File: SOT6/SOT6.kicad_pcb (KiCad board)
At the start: 2 copper layers, 11.4 x 8.9 mm, 5 parts, among them J1 Conn_01x03, J2 Conn_01x03

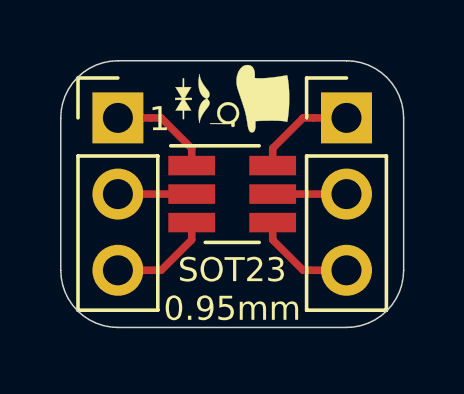
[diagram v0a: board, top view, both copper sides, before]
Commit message: Silkscreens and sizes updated
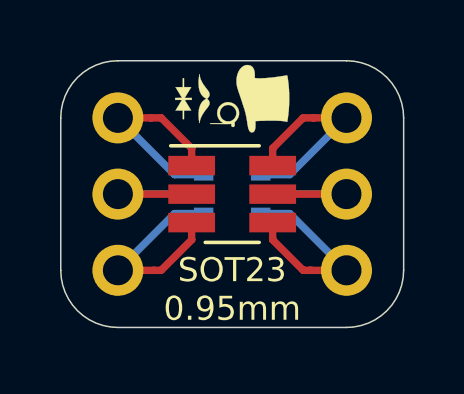
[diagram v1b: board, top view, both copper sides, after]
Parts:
- removed the G*** at (158.8, 96.5)
- added G***: LOGO, logo:logo38x53, B.Cu at (158.8, 93.3)
- added J4: Conn_02x03_Counter_Clockwise, Package_TO_SOT_SMD:SOT-363_SC-70-6, B.Cu at (158.8, 96.5)
- renumbered SOT23 to J3
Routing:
- net Net-(J2-Pad3): track 3.46 -> 7.10 mm
- net Net-(J2-Pad1): track 3.46 -> 7.10 mm
- net Net-(J1-Pad3): track 3.46 -> 7.10 mm
- net Net-(J1-Pad1): track 3.46 -> 7.10 mm
- net Net-(J2-Pad2): track 2.46 -> 5.32 mm
- net Net-(J1-Pad2): track 2.46 -> 5.32 mm
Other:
- board text added: "SC-70 0.65mm"
- board text removed: "1"

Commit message: Dimensions Added And TQFP64 Added
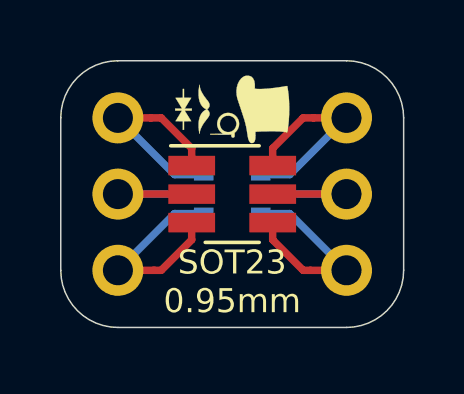
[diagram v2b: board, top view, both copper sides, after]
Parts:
- moved G*** 0.38 mm to (158.8, 93.7)
- moved G*** 0.36 mm to (158.8, 93.7)
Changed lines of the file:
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@@
   (general
     (thickness 1.6)
-    (drawings 12)
+    (drawings 14)
     (tracks 28)
     (zones 0)
@@
     (34 B.Paste user hide)
     (35 F.Paste user hide)
-    (36 B.SilkS user)
+    (36 B.SilkS user hide)
     (37 F.SilkS user)
     (38 B.Mask user hide)
@@
   )
   (module logo:logo38x53 (layer B.Cu)
-    (at 158.75 93.345 90)
+    (at 158.7754 93.726 90)
     (fp_text reference G*** (at 0 0 270) (layer B.SilkS) hide
       (effects (font (size 1.524 1.524) (thickness 0.3)) (justify mirror))
@@
   )
   (module logo:logo38x53 (layer F.Cu)
-    (at 158.75 93.345 270)
+    (at 158.75 93.7006 270)
     (fp_text reference G*** (at 0 0 90) (layer F.SilkS) hide
       (effects (font (size 1.524 1.524) (thickness 0.3)))
@@
     )
   )
+  (dimension 5.08 (width 0.15) (layer Dwgs.User)
+    (gr_text "5.080 mm" (at 168.305 96.52 270) (layer Dwgs.User)
+      (effects (font (size 1 1) (thickness 0.15)) hide)
+    )
+    (feature1 (pts (xy 162.56 99.06) (xy 167.591421 99.06)))
+    (feature2 (pts (xy 162.56 93.98) (xy 167.591421 93.98)))
+    (crossbar (pts (xy 167.005 93.98) (xy 167.005 99.06)))
+    (arrow1a (pts (xy 167.005 99.06) (xy 166.418579 97.933496)))
+    (arrow1b (pts (xy 167.005 99.06) (xy 167.591421 97.933496)))
+    (arrow2a (pts (xy 167.005 93.98) (xy 166.418579 95.106504)))
+    (arrow2b (pts (xy 167.005 93.98) (xy 167.591421 95.106504)))
+  )
+  (dimension 7.62 (width 0.15) (layer Dwgs.User)
+    (gr_text "7.620 mm" (at 158.75 88.743) (layer Dwgs.User)
+      (effects (font (size 1 1) (thickness 0.15)) hide)
+    )
+    (feature1 (pts (xy 162.56 93.98) (xy 162.56 89.456579)))
+    (feature2 (pts (xy 154.94 93.98) (xy 154.94 89.456579)))
+    (crossbar (pts (xy 154.94 90.043) (xy 162.56 90.043)))
+    (arrow1a (pts (xy 162.56 90.043) (xy 161.433496 90.629421)))
+    (arrow1b (pts (xy 162.56 90.043) (xy 161.433496 89.456579)))
+    (arrow2a (pts (xy 154.94 90.043) (xy 156.066504 90.629421)))
+    (arrow2b (pts (xy 154.94 90.043) (xy 156.066504 89.456579)))
+  )
   (dimension 8.89 (width 0.15) (layer Dwgs.User)
-    (gr_text "8.890 mm" (at 170.591 96.52 270) (layer Dwgs.User)
-      (effects (font (size 1 1) (thickness 0.15)))
-    )
-    (feature1 (pts (xy 164.465 100.965) (xy 169.877421 100.965)))
-    (feature2 (pts (xy 164.465 92.075) (xy 169.877421 92.075)))
-    (crossbar (pts (xy 169.291 92.075) (xy 169.291 100.965)))
-    (arrow1a (pts (xy 169.291 100.965) (xy 168.704579 99.838496)))
-    (arrow1b (pts (xy 169.291 100.965) (xy 169.877421 99.838496)))
-    (arrow2a (pts (xy 169.291 92.075) (xy 168.704579 93.201504)))
-    (arrow2b (pts (xy 169.291 92.075) (xy 169.877421 93.201504)))
+    (gr_text "8.890 mm" (at 171.353 96.52 270) (layer Dwgs.User)
+      (effects (font (size 1 1) (thickness 0.15)) hide)
+    )
+    (feature1 (pts (xy 162.56 100.965) (xy 170.639421 100.965)))
+    (feature2 (pts (xy 162.56 92.075) (xy 170.639421 92.075)))
+    (crossbar (pts (xy 170.053 92.075) (xy 170.053 100.965)))
+    (arrow1a (pts (xy 170.053 100.965) (xy 169.466579 99.838496)))
+    (arrow1b (pts (xy 170.053 100.965) (xy 170.639421 99.838496)))
+    (arrow2a (pts (xy 170.053 92.075) (xy 169.466579 93.201504)))
+    (arrow2b (pts (xy 170.053 92.075) (xy 170.639421 93.201504)))
   )
   (dimension 11.43 (width 0.15) (layer Dwgs.User)
-    (gr_text "11.430 mm" (at 158.75 86.711) (layer Dwgs.User)
-      (effects (font (size 1 1) (thickness 0.15)))
-    )
-    (feature1 (pts (xy 164.465 92.075) (xy 164.465 87.424579)))
-    (feature2 (pts (xy 153.035 92.075) (xy 153.035 87.424579)))
-    (crossbar (pts (xy 153.035 88.011) (xy 164.465 88.011)))
-    (arrow1a (pts (xy 164.465 88.011) (xy 163.338496 88.597421)))
-    (arrow1b (pts (xy 164.465 88.011) (xy 163.338496 87.424579)))
-    (arrow2a (pts (xy 153.035 88.011) (xy 154.161504 88.597421)))
-    (arrow2b (pts (xy 153.035 88.011) (xy 154.161504 87.424579)))
-  )
-  (gr_text "SC-70\n0.65mm" (at 158.75 99.695) (layer B.SilkS)
+    (gr_text "11.430 mm" (at 158.75 86.203) (layer Dwgs.User)
+      (effects (font (size 1 1) (thickness 0.15)) hide)
+    )
+    (feature1 (pts (xy 164.465 93.98) (xy 164.465 86.916579)))
+    (feature2 (pts (xy 153.035 93.98) (xy 153.035 86.916579)))
+    (crossbar (pts (xy 153.035 87.503) (xy 164.465 87.503)))
+    (arrow1a (pts (xy 164.465 87.503) (xy 163.338496 88.089421)))
+    (arrow1b (pts (xy 164.465 87.503) (xy 163.338496 86.916579)))
+    (arrow2a (pts (xy 153.035 87.503) (xy 154.161504 88.089421)))
+    (arrow2b (pts (xy 153.035 87.503) (xy 154.161504 86.916579)))
+  )
+  (gr_text "SC-70\n0.65mm" (at 158.7246 99.441) (layer B.SilkS)
     (effects (font (size 0.8 0.8) (thickness 0.15)) (justify mirror))
   )
-  (gr_text "SOT23\n0.95mm" (at 158.75 99.695) (layer F.SilkS)
+  (gr_text "SOT23\n0.95mm" (at 158.75 99.441) (layer F.SilkS)
     (effects (font (size 0.8 0.8) (thickness 0.15)))
   )

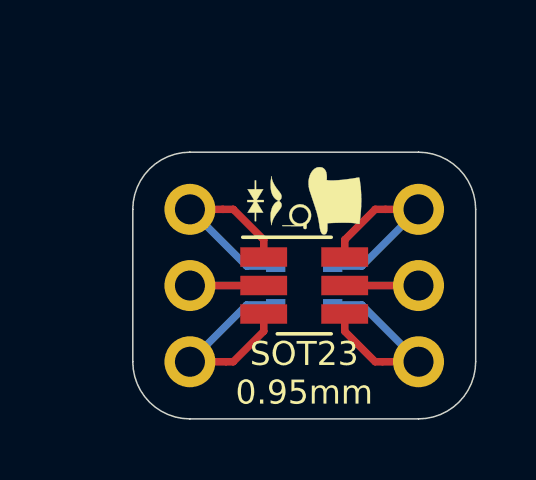
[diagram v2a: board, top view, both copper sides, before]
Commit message: Numbering Orientation Edited
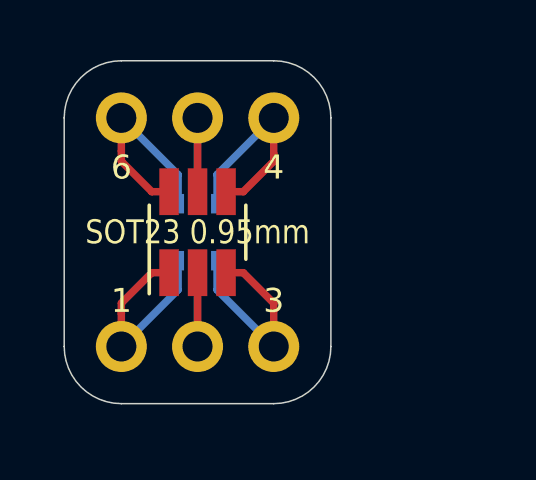
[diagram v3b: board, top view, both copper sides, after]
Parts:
- removed the G*** at (158.8, 93.7)
- moved J1 10.4 mm to (152.7, 90.9), turned to 90 degrees
- moved G*** 6.45 mm to (152.4, 94.7), turned to 180 degrees
- moved J2 5.11 mm to (152.7, 98.6), turned to 90 degrees
- moved J3 3.98 mm to (155.2, 94.7), turned to 90 degrees
- moved J4 3.98 mm to (155.2, 94.7), turned to 270 degrees
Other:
- board size 11.4 x 8.9 mm -> 8.9 x 11.4 mm
- board text added: "1"
- board text added: "3"
- board text added: "4"
- board text added: "6"

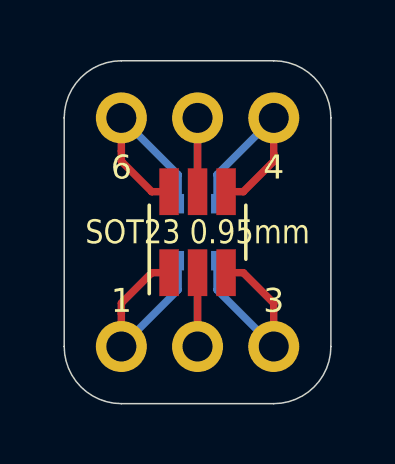
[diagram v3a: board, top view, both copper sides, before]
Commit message: Silkscreen Edits
Dimensions moved to Drawings Layer
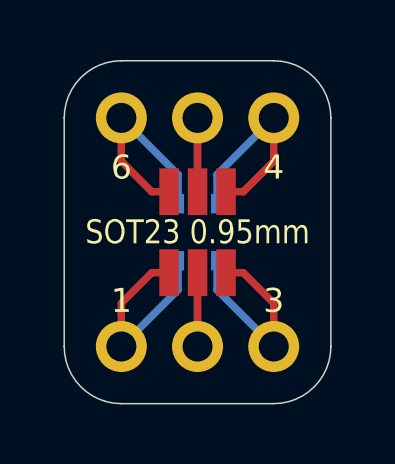
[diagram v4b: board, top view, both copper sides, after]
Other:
- rule pad_to_mask_clearance: 0.051 -> 0
- rule solder_mask_min_width: 0.25 -> 0.1
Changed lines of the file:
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@@
   (page A4)
   (layers
-    (0 F.Cu signal hide)
+    (0 F.Cu signal)
     (31 B.Cu signal)
     (32 B.Adhes user)
@@
     (pad_size 1.7 1.7)
     (pad_drill 1)
-    (pad_to_mask_clearance 0.051)
-    (solder_mask_min_width 0.25)
+    (pad_to_mask_clearance 0)
+    (solder_mask_min_width 0.1)
     (aux_axis_origin 0 0)
     (visible_elements 7FFFFFFF)
@@
       (usegerberadvancedattributes false)
       (creategerberjobfile false)
-      (excludeedgelayer false)
+      (excludeedgelayer true)
       (linewidth 0.100000)
       (plotframeref false)
       (viasonmask false)
       (mode 1)
-      (useauxorigin false)
+      (useauxorigin true)
       (hpglpennumber 1)
       (hpglpenspeed 20)
@@
       (drillshape 0)
       (scaleselection 1)
-      (outputdirectory "../../Gerbers/SOT23/"))
+      (outputdirectory "C:/Users/elisha3/Desktop/GitHub/Gerbers/SOT6/"))
   )
   (net 0 "")
@@
     (add_net "Net-(J2-Pad2)")
     (add_net "Net-(J2-Pad3)")
+  )
+  (module Package_TO_SOT_SMD:SOT-23-6_Handsoldering (layer F.Cu)
+    (at 155.194 94.742 90)
+    (descr "6-pin SOT-23 package, Handsoldering")
+    (tags "SOT-23-6 Handsoldering")
+    (attr smd)
+    (fp_text reference J3 (at 0 -2.9 90) (layer F.SilkS) hide
+      (effects (font (size 1 1) (thickness 0.15)))
+    )
+    (fp_text value Conn_02x03_Counter_Clockwise (at 0 2.9 90) (layer F.Fab)
+      (effects (font (size 1 1) (thickness 0.15)))
+    )
+    (fp_line (start 0.9 -1.55) (end 0.9 1.55) (layer F.Fab) (width 0.1))
+    (fp_line (start 0.9 1.55) (end -0.9 1.55) (layer F.Fab) (width 0.1))
+    (fp_line (start -0.9 -0.9) (end -0.9 1.55) (layer F.Fab) (width 0.1))
+    (fp_line (start 0.9 -1.55) (end -0.25 -1.55) (layer F.Fab) (width 0.1))
+    (fp_line (start -0.9 -0.9) (end -0.25 -1.55) (layer F.Fab) (width 0.1))
+    (fp_line (start -2.4 -1.8) (end 2.4 -1.8) (layer F.CrtYd) (width 0.05))
+    (fp_line (start 2.4 -1.8) (end 2.4 1.8) (layer F.CrtYd) (width 0.05))
+    (fp_line (start 2.4 1.8) (end -2.4 1.8) (layer F.CrtYd) (width 0.05))
+    (fp_line (start -2.4 1.8) (end -2.4 -1.8) (layer F.CrtYd) (width 0.05))
+    (fp_text user %R (at 0 0 180) (layer F.Fab)
+      (effects (font (size 0.5 0.5) (thickness 0.075)))
+    )
+    (pad 5 smd rect (at 1.35 0 90) (size 1.56 0.65) (layers F.Cu F.Paste F.Mask)
+      (net 2 "Net-(J1-Pad2)"))
+    (pad 6 smd rect (at 1.35 -0.95 90) (size 1.56 0.65) (layers F.Cu F.Paste F.Mask)
+      (net 3 "Net-(J1-Pad1)"))
+    (pad 4 smd rect (at 1.35 0.95 90) (size 1.56 0.65) (layers F.Cu F.Paste F.Mask)
+      (net 1 "Net-(J1-Pad3)"))
+    (pad 3 smd rect (at -1.35 0.95 90) (size 1.56 0.65) (layers F.Cu F.Paste F.Mask)
+      (net 4 "Net-(J2-Pad3)"))
+    (pad 2 smd rect (at -1.35 0 90) (size 1.56 0.65) (layers F.Cu F.Paste F.Mask)
+      (net 5 "Net-(J2-Pad2)"))
+    (pad 1 smd rect (at -1.35 -0.95 90) (size 1.56 0.65) (layers F.Cu F.Paste F.Mask)
+      (net 6 "Net-(J2-Pad1)"))
+    (model ${KISYS3DMOD}/Package_TO_SOT_SMD.3dshapes/SOT-23-6.wrl
+      (at (xyz 0 0 0))
+      (scale (xyz 1 1 1))
+      (rotate (xyz 0 0 0))
+    )
   )
   (module logo:logo38x53 (layer B.Cu)
@@
     )
   )
-  (module Package_TO_SOT_SMD:SOT-23-6_Handsoldering (layer F.Cu)
-    (at 155.194 94.742 90)
-    (descr "6-pin SOT-23 package, Handsoldering")
-    (tags "SOT-23-6 Handsoldering")
-    (attr smd)
-    (fp_text reference J3 (at 0 -2.9 90) (layer F.SilkS) hide
-      (effects (font (size 1 1) (thickness 0.15)))
-    )
-    (fp_text value Conn_02x03_Counter_Clockwise (at 0 2.9 90) (layer F.Fab)
-      (effects (font (size 1 1) (thickness 0.15)))
-    )
-    (fp_line (start 0.9 -1.55) (end 0.9 1.55) (layer F.Fab) (width 0.1))
-    (fp_line (start 0.9 1.55) (end -0.9 1.55) (layer F.Fab) (width 0.1))
-    (fp_line (start -0.9 -0.9) (end -0.9 1.55) (layer F.Fab) (width 0.1))
-    (fp_line (start 0.9 -1.55) (end -0.25 -1.55) (layer F.Fab) (width 0.1))
-    (fp_line (start -0.9 -0.9) (end -0.25 -1.55) (layer F.Fab) (width 0.1))
-    (fp_line (start -2.4 -1.8) (end 2.4 -1.8) (layer F.CrtYd) (width 0.05))
-    (fp_line (start 2.4 -1.8) (end 2.4 1.8) (layer F.CrtYd) (width 0.05))
-    (fp_line (start 2.4 1.8) (end -2.4 1.8) (layer F.CrtYd) (width 0.05))
-    (fp_line (start -2.4 1.8) (end -2.4 -1.8) (layer F.CrtYd) (width 0.05))
-    (fp_line (start 0.9 -1.61) (end -2.05 -1.61) (layer F.SilkS) (width 0.12))
-    (fp_line (start -0.9 1.61) (end 0.9 1.61) (layer F.SilkS) (width 0.12))
-    (fp_text user %R (at 0 0) (layer F.Fab)
-      (effects (font (size 0.5 0.5) (thickness 0.075)))
-    )
-    (pad 5 smd rect (at 1.35 0 90) (size 1.56 0.65) (layers F.Cu F.Paste F.Mask)
-      (net 2 "Net-(J1-Pad2)"))
-    (pad 6 smd rect (at 1.35 -0.95 90) (size 1.56 0.65) (layers F.Cu F.Paste F.Mask)
-      (net 3 "Net-(J1-Pad1)"))
-    (pad 4 smd rect (at 1.35 0.95 90) (size 1.56 0.65) (layers F.Cu F.Paste F.Mask)
-      (net 1 "Net-(J1-Pad3)"))
-    (pad 3 smd rect (at -1.35 0.95 90) (size 1.56 0.65) (layers F.Cu F.Paste F.Mask)
-      (net 4 "Net-(J2-Pad3)"))
-    (pad 2 smd rect (at -1.35 0 90) (size 1.56 0.65) (layers F.Cu F.Paste F.Mask)
-      (net 5 "Net-(J2-Pad2)"))
-    (pad 1 smd rect (at -1.35 -0.95 90) (size 1.56 0.65) (layers F.Cu F.Paste F.Mask)
-      (net 6 "Net-(J2-Pad1)"))
-    (model ${KISYS3DMOD}/Package_TO_SOT_SMD.3dshapes/SOT-23-6.wrl
-      (at (xyz 0 0 0))
-      (scale (xyz 1 1 1))
-      (rotate (xyz 0 0 0))
-    )
-  )
   (gr_text 6 (at 152.654 92.583) (layer F.SilkS)
     (effects (font (size 0.8 0.8) (thickness 0.13)))
@@
     (effects (font (size 0.8 0.8) (thickness 0.13)))
   )
-  (dimension 5.08 (width 0.15) (layer F.SilkS)
-    (gr_text "5.080 mm" (at 155.194 85.187) (layer F.SilkS)
+  (dimension 5.08 (width 0.15) (layer Dwgs.User)
+    (gr_text "5.080 mm" (at 155.194 85.187) (layer Dwgs.User)
       (effects (font (size 1 1) (thickness 0.15)) hide)
     )
@@
     (arrow2b (pts (xy 152.654 86.487) (xy 153.780504 85.900579)))
   )
-  (dimension 7.62 (width 0.15) (layer F.SilkS)
-    (gr_text "7.620 mm" (at 147.417 94.742 90) (layer F.SilkS)
+  (dimension 7.62 (width 0.15) (layer Dwgs.User)
+    (gr_text "7.620 mm" (at 147.417 94.742 90) (layer Dwgs.User)
       (effects (font (size 1 1) (thickness 0.15)) hide)
     )
@@
     (arrow2b (pts (xy 148.717 98.552) (xy 148.130579 97.425496)))
   )
-  (dimension 8.89 (width 0.15) (layer F.SilkS)
-    (gr_text "8.890 mm" (at 155.194 82.139) (layer F.SilkS)
+  (dimension 8.89 (width 0.15) (layer Dwgs.User)
+    (gr_text "8.890 mm" (at 155.194 82.139) (layer Dwgs.User)
       (effects (font (size 1 1) (thickness 0.15)) hide)
     )
@@
     (arrow2b (pts (xy 150.749 83.439) (xy 151.875504 82.852579)))
   )
-  (dimension 11.43 (width 0.15) (layer F.SilkS)
-    (gr_text "11.430 mm" (at 144.877 94.742 90) (layer F.SilkS)
+  (dimension 11.43 (width 0.15) (layer Dwgs.User)
+    (gr_text "11.430 mm" (at 144.877 94.742 90) (layer Dwgs.User)
       (effects (font (size 1 1) (thickness 0.15)) hide)
     )

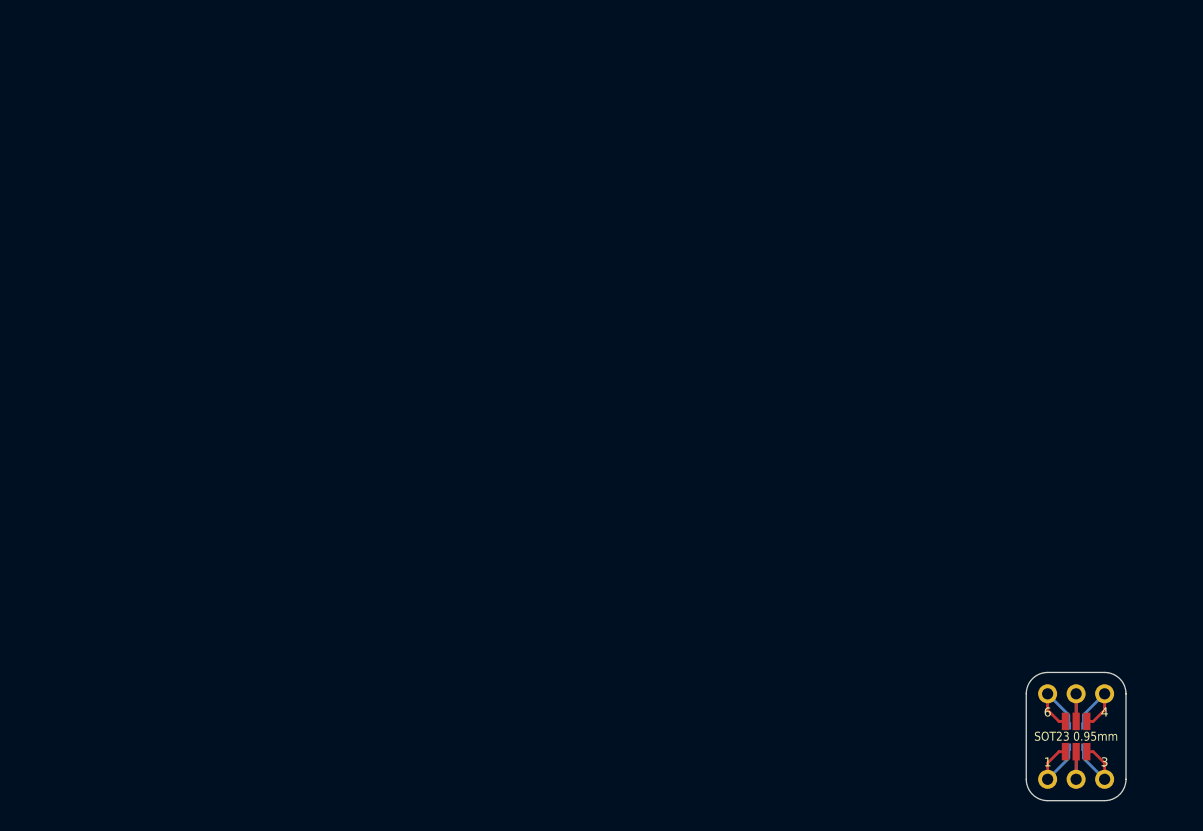
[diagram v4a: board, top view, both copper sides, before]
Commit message: USB, SD and CR Cells Added
MicroSD, MicroUSB, MiniUSB, USB-C, CR1220, CR2032 added as well as all schematics page sizes optimised
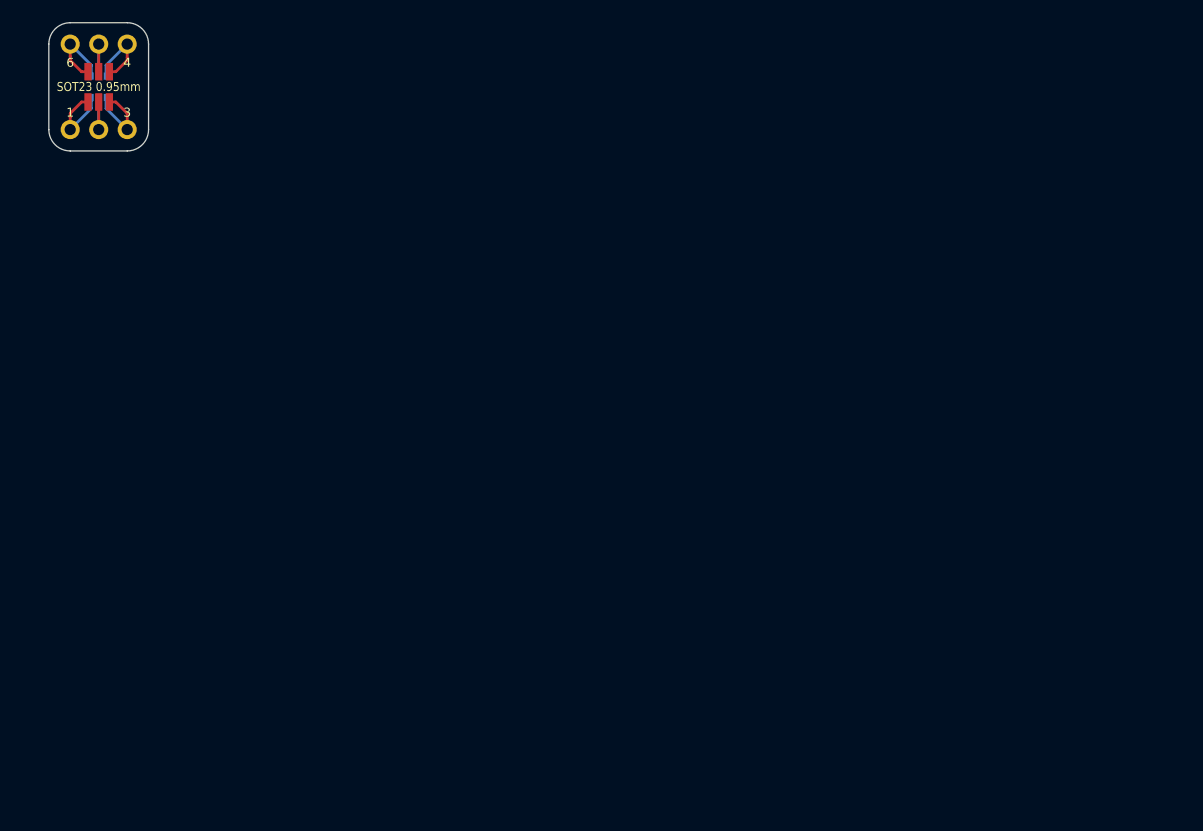
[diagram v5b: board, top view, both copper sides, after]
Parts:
- moved J2 104.6 mm to (65.5, 40.6)
- moved G*** 104.6 mm to (65.3, 36.8)
- moved J1 104.6 mm to (65.5, 33.0)
- moved J3 104.6 mm to (68.1, 36.8)
- moved J4 104.6 mm to (68.1, 36.8)
